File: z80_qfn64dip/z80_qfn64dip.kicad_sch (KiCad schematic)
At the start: 48 parts, among them J1 Conn_02x04_Odd_Even, U1 Caravel_QFN, U2 Z80CPU, U3 AZ1117-3.3, U4 AP2112K-1.8, U6 AT25EU0081A, X1 10MHz

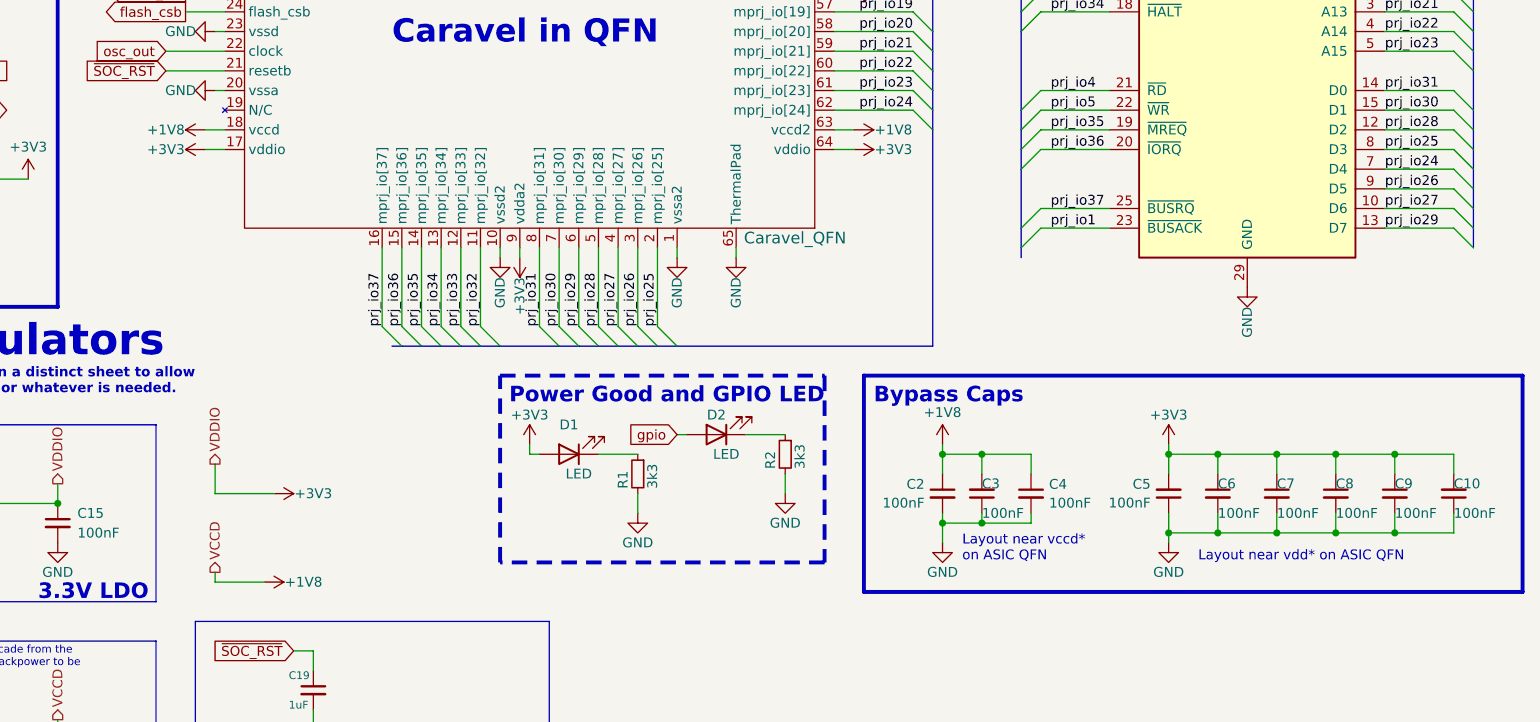
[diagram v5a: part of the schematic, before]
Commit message: layout tweaks, update to kicad 9
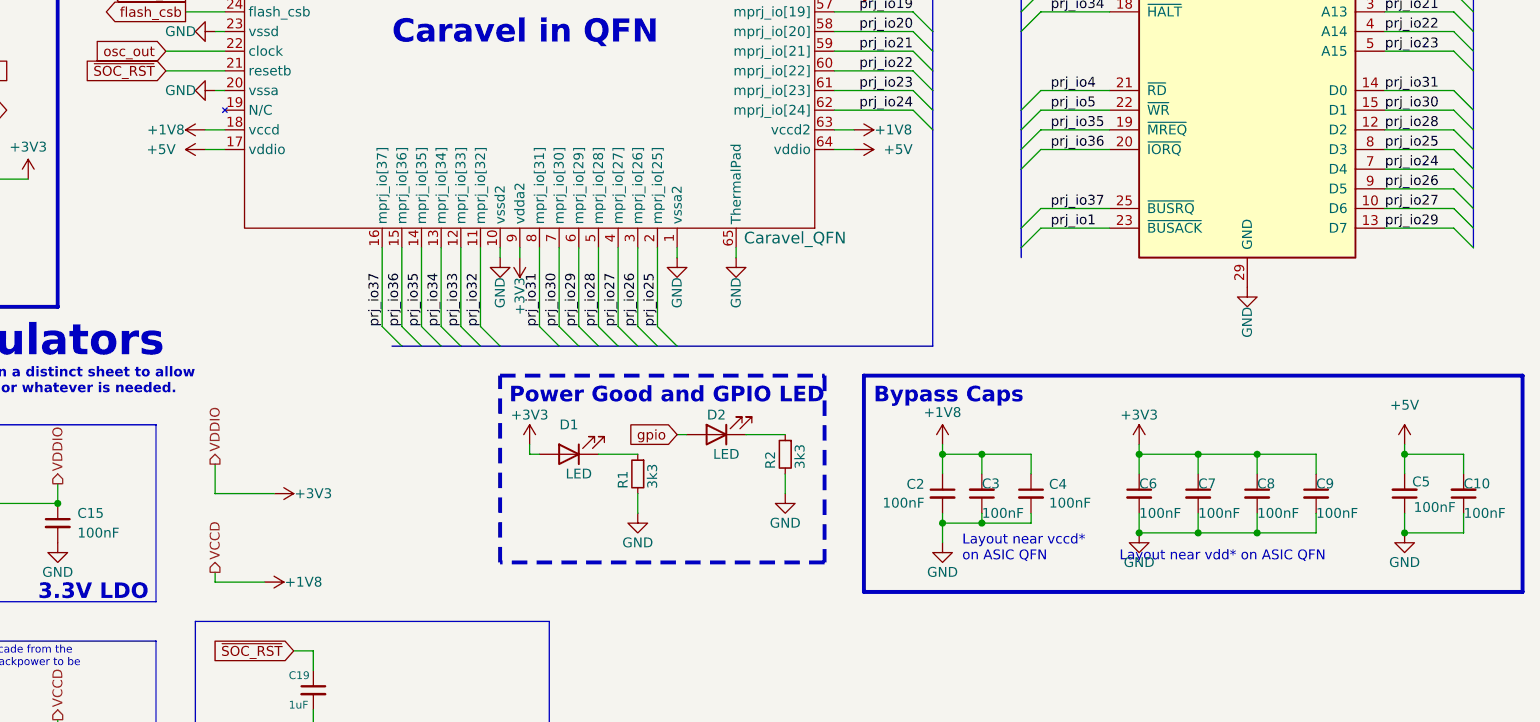
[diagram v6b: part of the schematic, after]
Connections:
- net +3V3: no longer C10.2, C5.2, U1.17 (vddio), U1.64 (vddio)
- net +5V: now also C10.2, C5.2, U1.17 (vddio), U1.64 (vddio)
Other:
- moved on the sheet: C6, C7, C8, C9

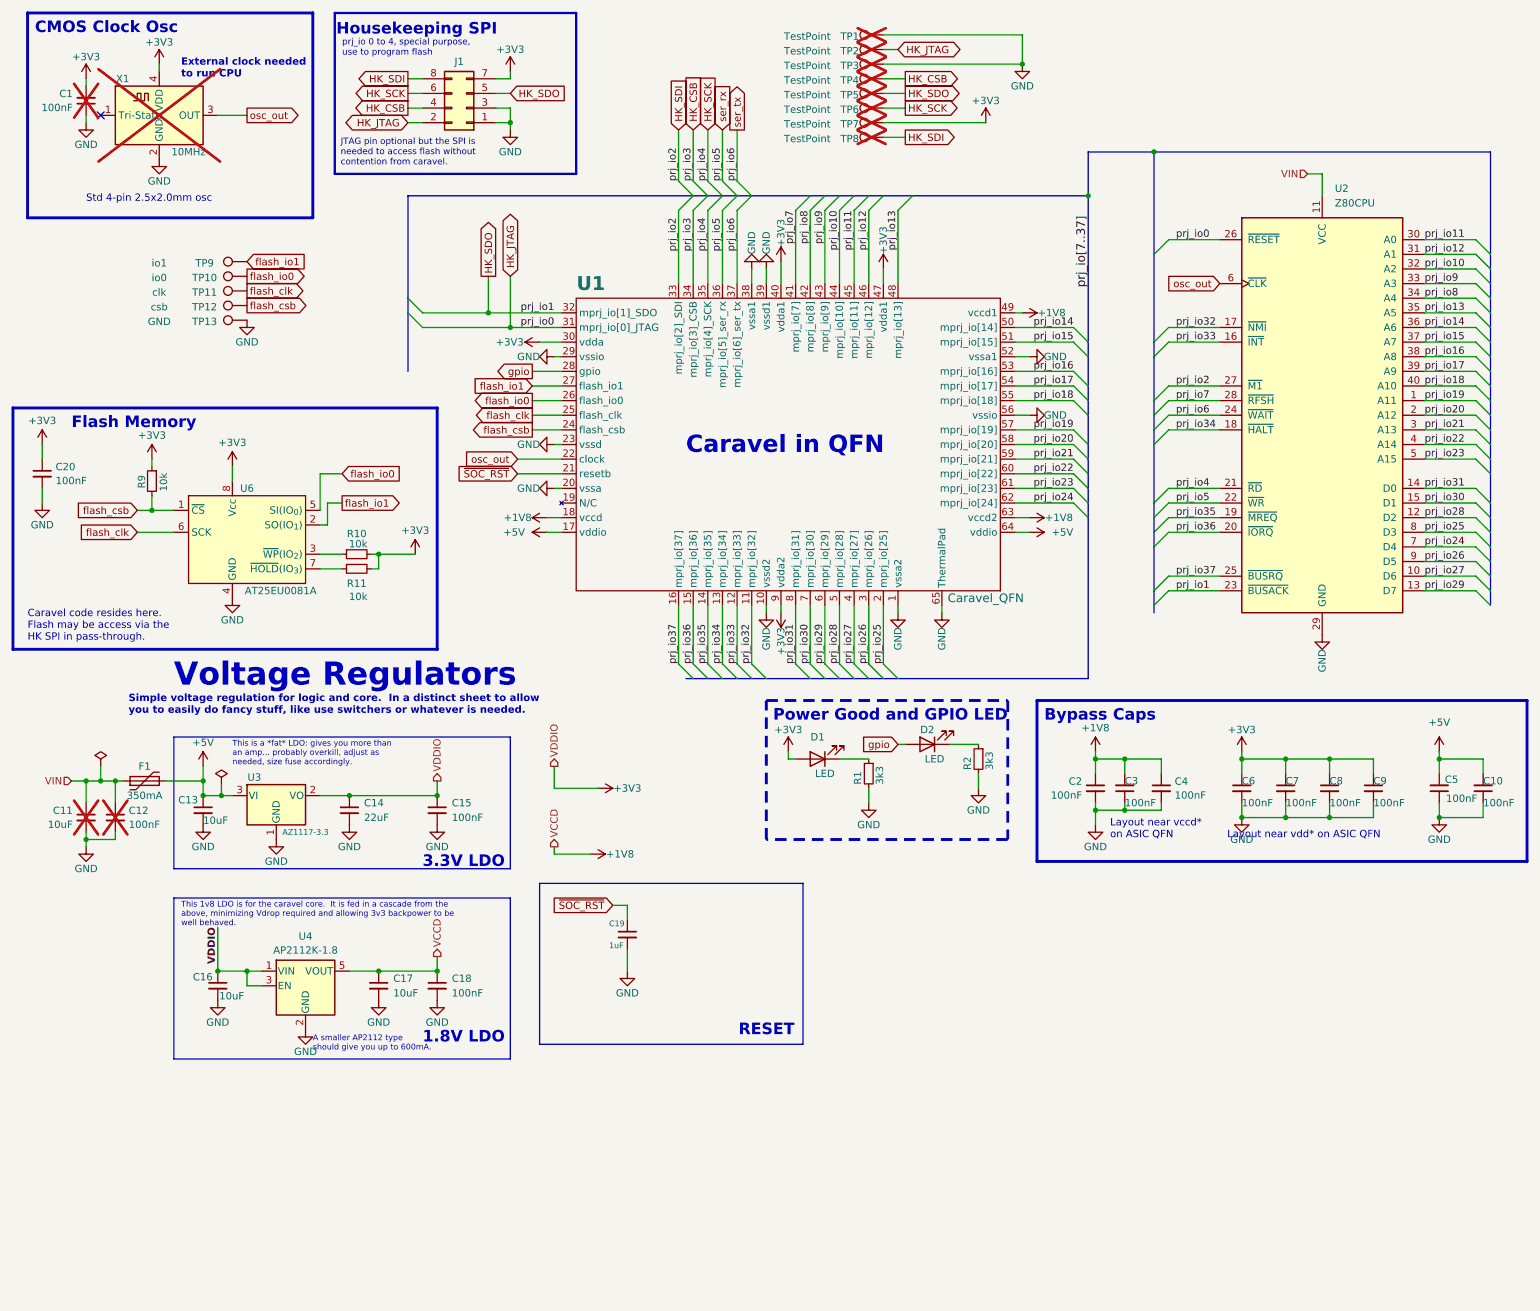
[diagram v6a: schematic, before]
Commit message: routed and DRC mostly checked
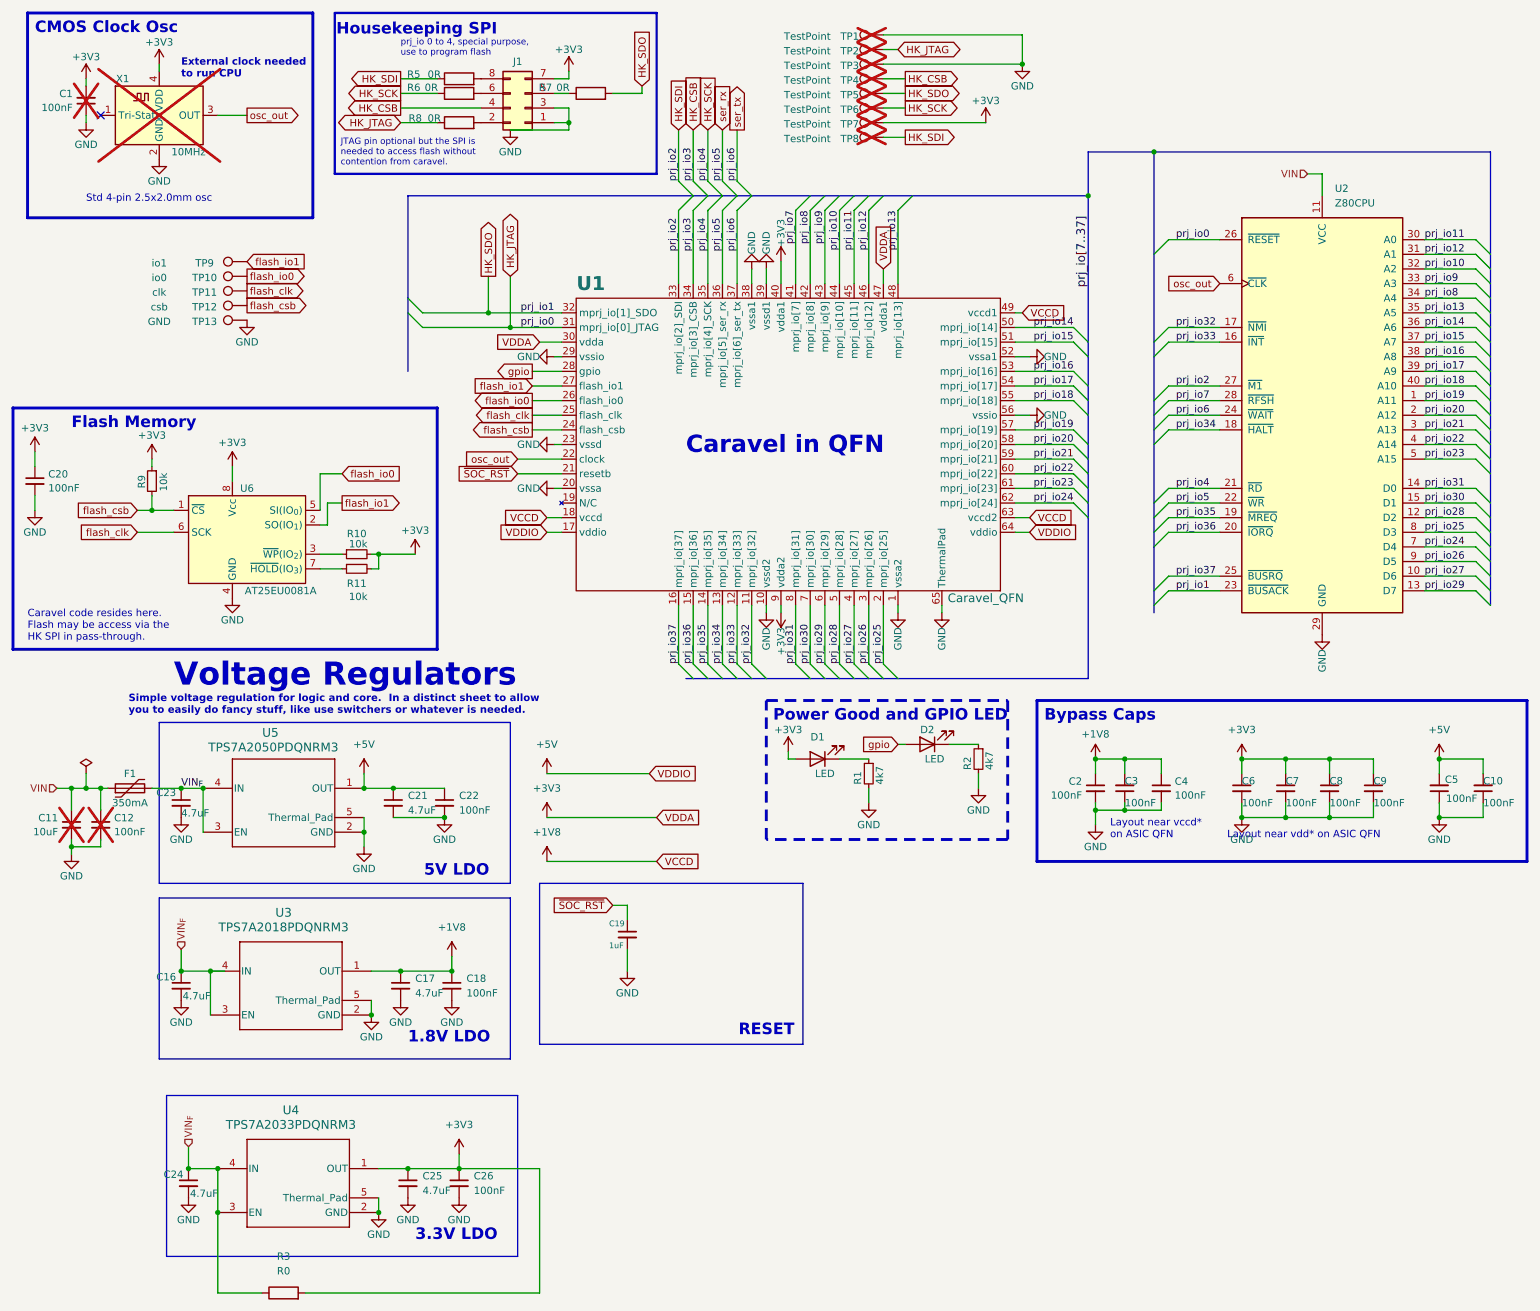
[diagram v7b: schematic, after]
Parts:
- removed C13: 10uF, Capacitor_SMD:C_0805_2012Metric, symbol Device:C_Small
- removed C14: 22uF, Capacitor_SMD:C_0805_2012Metric, symbol Device:C_Small
- removed C15: 100nF, Capacitor_SMD:C_0603_1608Metric, symbol Device:C_Small
- removed U3: AZ1117-3.3, Package_TO_SOT_SMD:SOT-223-3_TabPin2, symbol Regulator_Linear:AZ1117-3.3
- removed U4: AP2112K-1.8, Package_TO_SOT_SMD:SOT-23-5, symbol Regulator_Linear:AP2112K-1.8
- added C21, C25: 4.7uF, Capacitor_SMD:C_0402_1005Metric, symbol Device:C_Small
- added C22, C26: 100nF, Capacitor_SMD:C_0402_1005Metric, symbol Device:C_Small
- added C23, C24: 4.7uF, Capacitor_SMD:C_0603_1608Metric, symbol Device:C_Small
- added R3: R0, Resistor_SMD:R_0603_1608Metric_Pad0.98x0.95mm_HandSolder, symbol Device:R
- added R5, R6, R7, R8: 0R, Resistor_SMD:R_0402_1005Metric_Pad0.72x0.64mm_HandSolder, symbol Device:R
- added U3: TPS7A2018PDQNRM3, KiCadModels:DQN0004A-MFG, symbol tps7a2018:TPS7A2018PDQNRM3
- added U4: TPS7A2033PDQNRM3, KiCadModels:DQN0004A-MFG, symbol tps7a2033:TPS7A2033PDQNRM3
- added U5: TPS7A2050PDQNRM3, KiCadModels:DQN0004A-MFG, symbol tps7a2050:TPS7A2050PDQNRM3
- C16: value 10uF -> 4.7uF; footprint Capacitor_SMD:C_0805_2012Metric -> Capacitor_SMD:C_0603_1608Metric
- C17: value 10uF -> 4.7uF; footprint Capacitor_SMD:C_0805_2012Metric -> Capacitor_SMD:C_0402_1005Metric
- C18, C19, C3: footprint Capacitor_SMD:C_0603_1608Metric -> Capacitor_SMD:C_0402_1005Metric
- C2, C20: footprint Capacitor_SMD:C_0603_1608Metric_Pad1.08x0.95mm_HandSolder -> Capacitor_SMD:C_0402_1005Metric_Pad0.74x0.62mm_HandSolder
- C4: footprint Capacitor_SMD:C_0603_1608Metric -> Capacitor_SMD:C_0402_1005Metric_Pad0.74x0.62mm_HandSolder
- J1: value Conn_02x04_Odd_Even -> Conn_08; footprint Connector_PinHeader_1.27mm:PinHeader_2x04_P1.27mm_Vertical -> Connector_JST:JST_SH_BM08B-SRSS-TB_1x08-1MP_P1.00mm_Vertical
- R1, R2: value 3k3 -> 4k7; footprint Resistor_SMD:R_0603_1608Metric -> Resistor_SMD:R_0402_1005Metric
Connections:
- net +1V8: now also U3.1 (OUT)
- net +3V3: now also C25.1, C26.1, R3.2, U4.1 (OUT); no longer C16.1
- net +5V: now also C21.1, C22.1, U5.1 (OUT); no longer F1.2
- net GND: now also C21.2, C22.2, C23.2, C24.2, C25.2, C26.2, U3.2 (GND), U3.5 (Thermal_Pad), U4.2 (GND), U4.5 (Thermal_Pad), U5.2 (GND), U5.5 (Thermal_Pad)
- net HK_JTAG: now also R8.1; no longer J1.2 (Pin_2)
- net HK_SCK: now also R6.1; no longer J1.6 (Pin_6)
- net HK_SDI: now also R5.1; no longer J1.8 (Pin_8)
- net HK_SDO: now also R7.2; no longer J1.5 (Pin_5)
- new net: J1.5 (Pin_5), R7.1
- new net: J1.8 (Pin_8), R5.2
- new net: J1.2 (Pin_2), R8.2
- new net: J1.6 (Pin_6), R6.2
- new net VIN_{F}: C16.1, C23.1, C24.1, F1.2, R3.1, U3.3 (EN), U3.4 (IN), U4.3 (EN), U4.4 (IN), U5.3 (EN), U5.4 (IN)
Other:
- note added: "5V LDO"
- note removed: "A smaller AP2112 type should give you up to 600mA."
- note removed: "This 1v8 LDO is for the caravel core. It is fed in a cascade from the above, minimizing Vdrop required and allowing 3v3 backpower to be well behaved."
- note removed: "This is a *fat* LDO: gives you more than an amp... probably overkill, adjust as needed, size fuse accordingly."
- moved on the sheet: C11, C12, C16, C17, C18, C20, F1, J1
